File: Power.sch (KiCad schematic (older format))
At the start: 13 parts

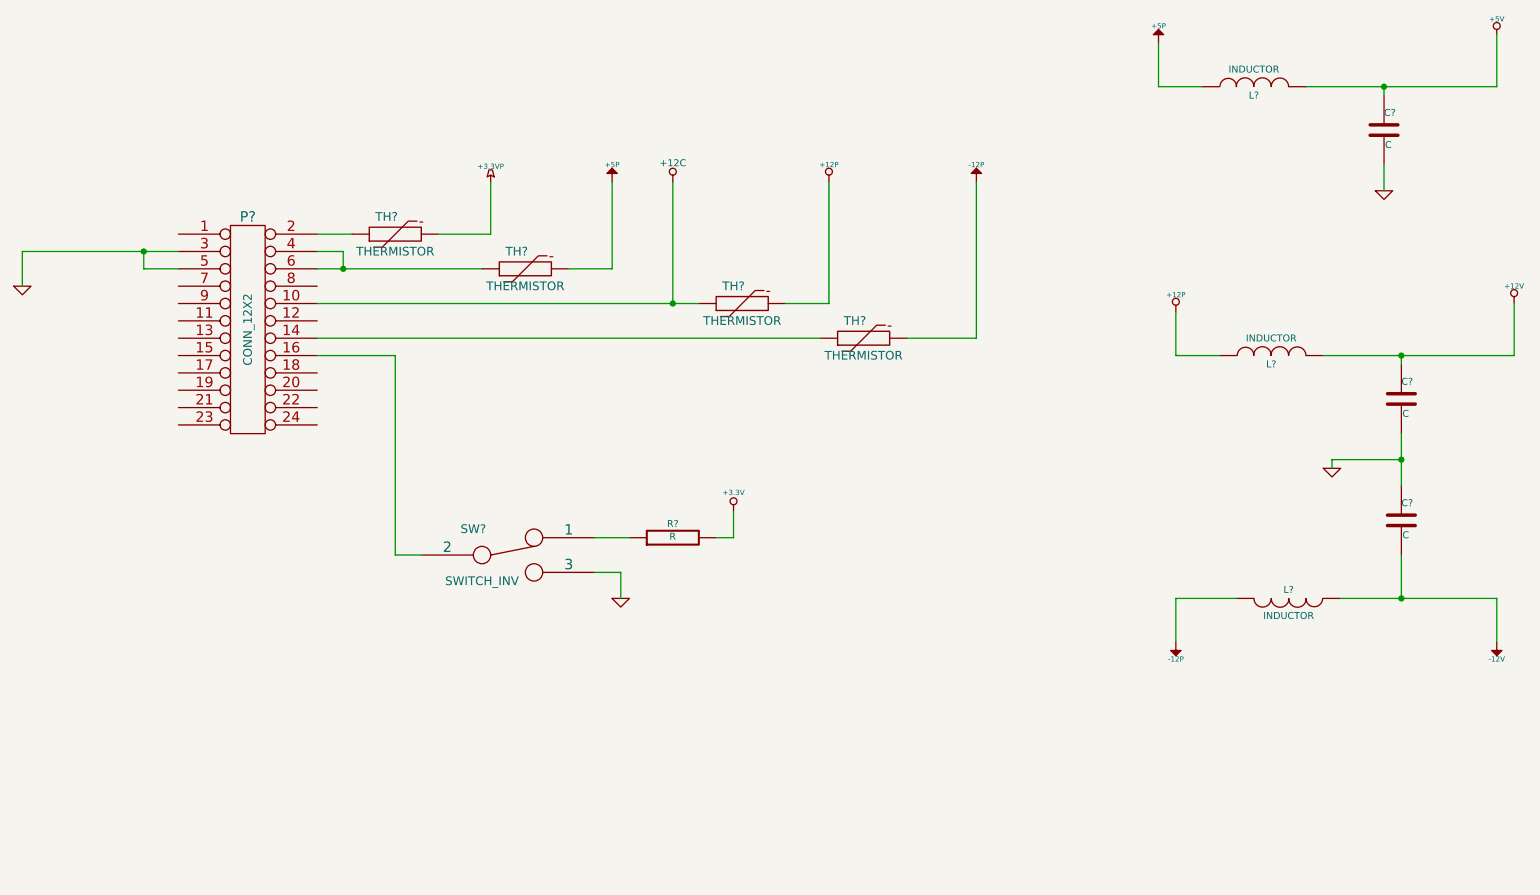
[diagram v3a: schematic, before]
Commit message: Relay module association and placement
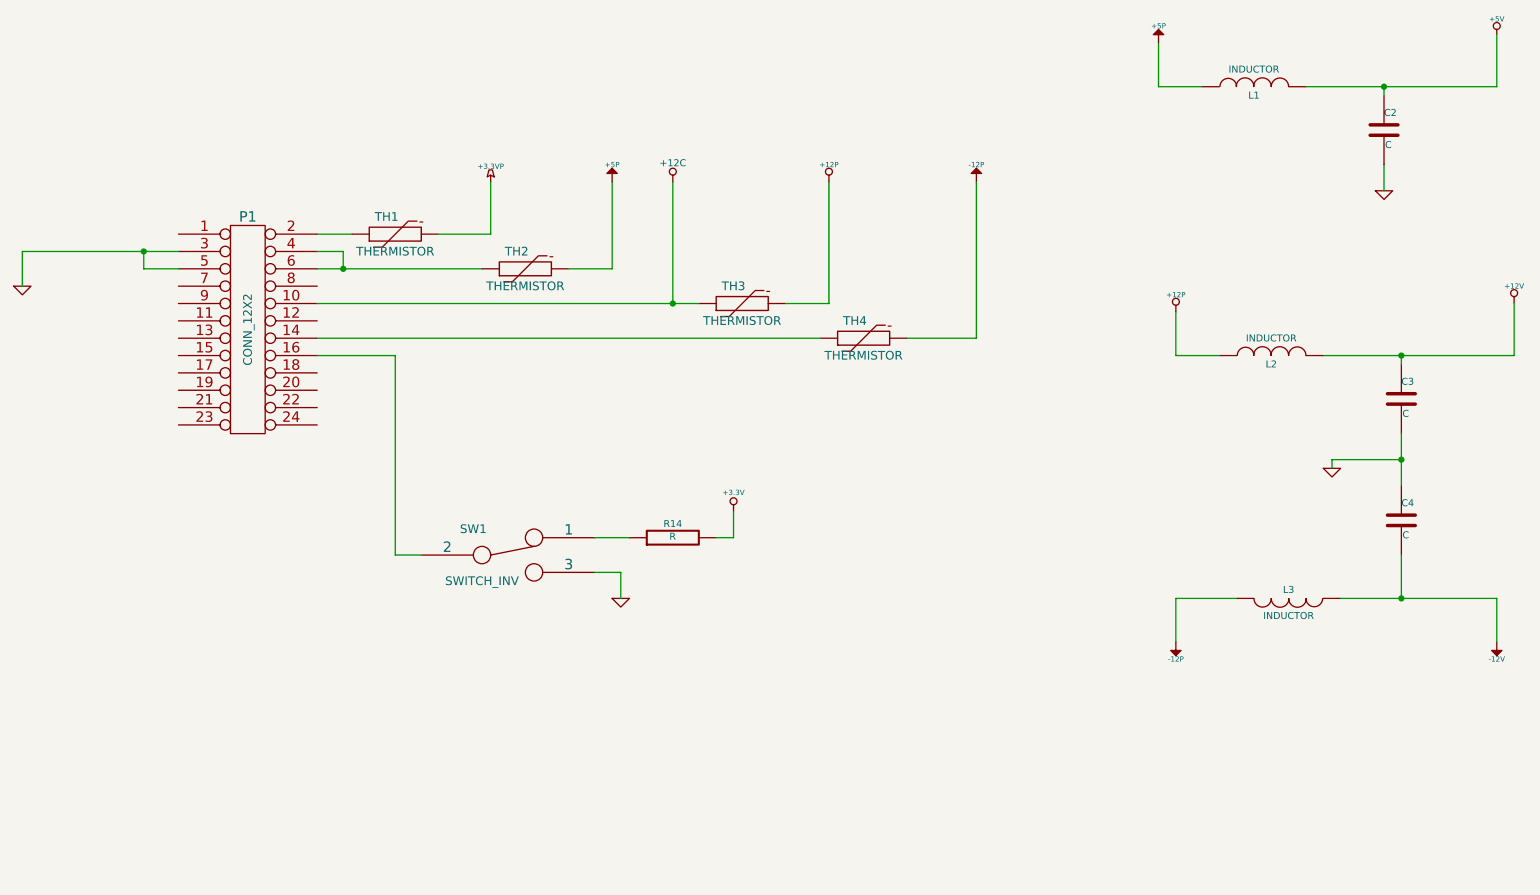
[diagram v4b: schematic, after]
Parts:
- gave numbers to parts that had none: 13
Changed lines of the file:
@@
 Sheet 4 9
 Title ""
-Date "18 feb 2014"
+Date "20 feb 2014"
 Rev ""
 Comp ""
@@
 $EndDescr
 $Comp
-L CONN_12X2 P?
+L CONN_12X2 P1
 U 1 1 52F67DF4
 P 2900 2400
-F 0 "P?" H 2900 3050 60  0000 C CNN
+F 0 "P1" H 2900 3050 60  0000 C CNN
 F 1 "CONN_12X2" V 2900 2400 50  0000 C CNN
 F 2 "" H 2900 2400 60  0000 C CNN
@@
 $EndComp
 $Comp
-L GND #PWR?
+L GND #PWR011
 U 1 1 52F67E5D
 P 1600 2150
-F 0 "#PWR?" H 1600 2150 30  0001 C CNN
+F 0 "#PWR011" H 1600 2150 30  0001 C CNN
 F 1 "GND" H 1600 2080 30  0001 C CNN
 F 2 "" H 1600 2150 60  0000 C CNN
@@
 $EndComp
 $Comp
-L SWITCH_INV SW?
+L SWITCH_INV SW1
 U 1 1 52F67EC9
 P 4400 3700
-F 0 "SW?" H 4200 3850 50  0000 C CNN
+F 0 "SW1" H 4200 3850 50  0000 C CNN
 F 1 "SWITCH_INV" H 4250 3550 50  0000 C CNN
 F 2 "~" H 4400 3700 60  0000 C CNN
@@
 	7100 2450 6700 2450
 $Comp
-L +12P #PWR?
+L +12P #PWR012
 U 1 1 52F68365
 P 6250 1550
-F 0 "#PWR?" H 6250 1520 30  0001 C CNN
+F 0 "#PWR012" H 6250 1520 30  0001 C CNN
 F 1 "+12P" H 6250 1650 30  0000 C CNN
 F 2 "" H 6250 1550 60  0000 C CNN
@@
 $EndComp
 $Comp
-L -12P #PWR?
+L -12P #PWR013
 U 1 1 52F68398
 P 7100 1550
-F 0 "#PWR?" H 7100 1680 20  0001 C CNN
+F 0 "#PWR013" H 7100 1680 20  0001 C CNN
 F 1 "-12P" H 7100 1650 30  0000 C CNN
 F 2 "" H 7100 1550 60  0000 C CNN
@@
 	3750 3700 3900 3700
 $Comp
-L GND #PWR?
+L GND #PWR014
 U 1 1 52F6840F
 P 5050 3950
-F 0 "#PWR?" H 5050 3950 30  0001 C CNN
+F 0 "#PWR014" H 5050 3950 30  0001 C CNN
 F 1 "GND" H 5050 3880 30  0001 C CNN
 F 2 "" H 5050 3950 60  0000 C CNN
@@
 	5050 3800 5050 3950
 $Comp
-L R R?
+L R R14
 U 1 1 52F6842F
 P 5350 3600
-F 0 "R?" V 5430 3600 40  0000 C CNN
+F 0 "R14" V 5430 3600 40  0000 C CNN
 F 1 "R" V 5357 3601 40  0000 C CNN
 F 2 "~" V 5280 3600 30  0000 C CNN
@@
 	3750 2550 3750 3700
 $Comp
-L +3.3V #PWR?
+L +3.3V #PWR015
 U 1 1 52F684A9
 P 5700 3450
-F 0 "#PWR?" H 5700 3410 30  0001 C CNN
+F 0 "#PWR015" H 5700 3410 30  0001 C CNN
 F 1 "+3.3V" H 5700 3560 30  0000 C CNN
 F 2 "" H 5700 3450 60  0000 C CNN
@@
 	5700 3600 5700 3450
 $Comp
-L +12P #PWR?
+L +12P #PWR016
 U 1 1 52F684CA
 P 8250 2300
-F 0 "#PWR?" H 8250 2270 30  0001 C CNN
+F 0 "#PWR016" H 8250 2270 30  0001 C CNN
 F 1 "+12P" H 8250 2400 30  0000 C CNN
 F 2 "" H 8250 2300 60  0000 C CNN
@@
 $EndComp
 $Comp
-L GND #PWR?
+L GND #PWR017
 U 1 1 52F684D0
 P 9150 3200
-F 0 "#PWR?" H 9150 3200 30  0001 C CNN
+F 0 "#PWR017" H 9150 3200 30  0001 C CNN
 F 1 "GND" H 9150 3130 30  0001 C CNN
 F 2 "" H 9150 3200 60  0000 C CNN
@@
 $EndComp
 $Comp
-L -12P #PWR?
+L -12P #PWR018
 U 1 1 52F684D6
 P 8250 4200
-F 0 "#PWR?" H 8250 4330 20  0001 C CNN
+F 0 "#PWR018" H 8250 4330 20  0001 C CNN
 F 1 "-12P" H 8250 4300 30  0000 C CNN
 F 2 "" H 8250 4200 60  0000 C CNN
@@
 $EndComp
 $Comp
-L INDUCTOR L?
+L INDUCTOR L2
 U 1 1 52F684DE
 P 8800 2550
-F 0 "L?" V 8750 2550 40  0000 C CNN
+F 0 "L2" V 8750 2550 40  0000 C CNN
 F 1 "INDUCTOR" V 8900 2550 40  0000 C CNN
 F 2 "~" H 8800 2550 60  0000 C CNN
@@
 $EndComp
 $Comp
-L INDUCTOR L?
+L INDUCTOR L3
 U 1 1 52F684EB
 P 8900 3950
-F 0 "L?" V 8850 3950 40  0000 C CNN
+F 0 "L3" V 8850 3950 40  0000 C CNN
 F 1 "INDUCTOR" V 9000 3950 40  0000 C CNN
 F 2 "~" H 8900 3950 60  0000 C CNN
@@
 $EndComp
 $Comp
-L C C?
+L C C3
 U 1 1 52F68508
 P 9550 2800
-F 0 "C?" H 9550 2900 40  0000 L CNN
+F 0 "C3" H 9550 2900 40  0000 L CNN
 F 1 "C" H 9556 2715 40  0000 L CNN
 F 2 "~" H 9588 2650 30  0000 C CNN
@@
 $EndComp
 $Comp
-L C C?
+L C C4
 U 1 1 52F68515
 P 9550 3500
-F 0 "C?" H 9550 3600 40  0000 L CNN
+F 0 "C4" H 9550 3600 40  0000 L CNN
 F 1 "C" H 9556 3415 40  0000 L CNN
 F 2 "~" H 9588 3350 30  0000 C CNN
@@
 	8250 3950 8600 3950
 $Comp
-L -12V #PWR?
+L -12V #PWR019
 U 1 1 52F68656
 P 10100 4200
-F 0 "#PWR?" H 10100 4330 20  0001 C CNN
+F 0 "#PWR019" H 10100 4330 20  0001 C CNN
 F 1 "-12V" H 10100 4300 30  0000 C CNN
 F 2 "" H 10100 4200 60  0000 C CNN
@@
 $EndComp
 $Comp
-L +12V #PWR?
+L +12V #PWR020
 U 1 1 52F68665
 P 10200 2250
-F 0 "#PWR?" H 10200 2200 20  0001 C CNN
+F 0 "#PWR020" H 10200 2200 20  0001 C CNN
 F 1 "+12V" H 10200 2350 30  0000 C CNN
 F 2 "" H 10200 2250 60  0000 C CNN
@@
 Connection ~ 9550 3950
 $Comp
-L +12C #PWR?
+L +12C #PWR021
 U 1 1 52F7CE7C
 P 5350 1550
-F 0 "#PWR?" H 5350 1520 30  0001 C CNN
+F 0 "#PWR021" H 5350 1520 30  0001 C CNN
 F 1 "+12C" H 5350 1660 40  0000 C CNN
 F 2 "" H 5350 1550 60  0000 C CNN
@@
 Connection ~ 5350 2250
 $Comp
-L THERMISTOR TH?
+L THERMISTOR TH1
 U 1 1 52F7D3F0
 P 3750 1850
-F 0 "TH?" V 3850 1900 50  0000 C CNN
+F 0 "TH1" V 3850 1900 50  0000 C CNN
 F 1 "THERMISTOR" V 3650 1850 50  0000 C CNN
 F 2 "~" H 3750 1850 60  0000 C CNN
@@
 $EndComp
 $Comp
-L THERMISTOR TH?
+L THERMISTOR TH2
 U 1 1 52F7D3FF
 P 4500 2050
-F 0 "TH?" V 4600 2100 50  0000 C CNN
+F 0 "TH2" V 4600 2100 50  0000 C CNN
 F 1 "THERMISTOR" V 4400 2050 50  0000 C CNN
 F 2 "~" H 4500 2050 60  0000 C CNN
@@
 $EndComp
 $Comp
-L THERMISTOR TH?
+L THERMISTOR TH3
 U 1 1 52F7D40E
 P 5750 2250
-F 0 "TH?" V 5850 2300 50  0000 C CNN
+F 0 "TH3" V 5850 2300 50  0000 C CNN
 F 1 "THERMISTOR" V 5650 2250 50  0000 C CNN
 F 2 "~" H 5750 2250 60  0000 C CNN
@@
 $EndComp
 $Comp
-L THERMISTOR TH?
+L THERMISTOR TH4
 U 1 1 52F7D41D
 P 6450 2450
-F 0 "TH?" V 6550 2500 50  0000 C CNN
+F 0 "TH4" V 6550 2500 50  0000 C CNN
 F 1 "THERMISTOR" V 6350 2450 50  0000 C CNN
 F 2 "~" H 6450 2450 60  0000 C CNN
@@
 $EndComp
 $Comp
-L +5P #PWR?
+L +5P #PWR13
 U 1 1 5302A929
 P 5000 1550
-F 0 "#PWR?" H 5000 1680 20  0001 C CNN
+F 0 "#PWR13" H 5000 1680 20  0001 C CNN
 F 1 "+5P" H 5000 1650 30  0000 C CNN
 F 2 "" H 5000 1550 60  0000 C CNN
@@
 $EndComp
 $Comp
-L +3.3VP #PWR?
+L +3.3VP #PWR022
 U 1 1 5302A942
 P 4300 1550
-F 0 "#PWR?" H 4350 1580 20  0001 C CNN
+F 0 "#PWR022" H 4350 1580 20  0001 C CNN
 F 1 "+3.3VP" H 4300 1640 30  0000 C CNN
 F 2 "" H 4300 1550 60  0000 C CNN
@@
 $EndComp
 $Comp
-L INDUCTOR L?
+L INDUCTOR L1
 U 1 1 5302A984
 P 8700 1000
-F 0 "L?" V 8650 1000 40  0000 C CNN
+F 0 "L1" V 8650 1000 40  0000 C CNN
 F 1 "INDUCTOR" V 8800 1000 40  0000 C CNN
 F 2 "~" H 8700 1000 60  0000 C CNN
@@
 $EndComp
 $Comp
-L C C?
+L C C2
 U 1 1 5302A98A
 P 9450 1250
-F 0 "C?" H 9450 1350 40  0000 L CNN
+F 0 "C2" H 9450 1350 40  0000 L CNN
 F 1 "C" H 9456 1165 40  0000 L CNN
 F 2 "~" H 9488 1100 30  0000 C CNN
@@
 Connection ~ 9450 1000
 $Comp
-L GND #PWR?
+L GND #PWR023
 U 1 1 5302A99D
 P 9450 1600
-F 0 "#PWR?" H 9450 1600 30  0001 C CNN
+F 0 "#PWR023" H 9450 1600 30  0001 C CNN
 F 1 "GND" H 9450 1530 30  0001 C CNN
 F 2 "" H 9450 1600 60  0000 C CNN
@@
 	9450 1600 9450 1450
 $Comp
-L +5P #PWR?
+L +5P #PWR19
 U 1 1 5302A9DA
 P 8150 750
-F 0 "#PWR?" H 8150 880 20  0001 C CNN
+F 0 "#PWR19" H 8150 880 20  0001 C CNN
 F 1 "+5P" H 8150 850 30  0000 C CNN
 F 2 "" H 8150 750 60  0000 C CNN
@@
 $EndComp
 $Comp
-L +5V #PWR?
+L +5V #PWR024
 U 1 1 5302A9E9
 P 10100 700
-F 0 "#PWR?" H 10100 790 20  0001 C CNN
+F 0 "#PWR024" H 10100 790 20  0001 C CNN
 F 1 "+5V" H 10100 790 30  0000 C CNN
 F 2 "" H 10100 700 60  0000 C CNN

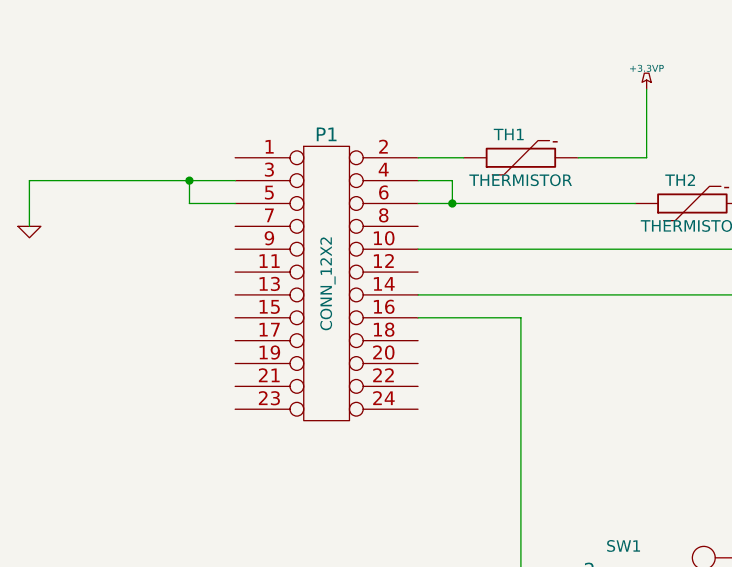
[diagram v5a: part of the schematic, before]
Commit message: Terminal block and Arduino: assc/placement
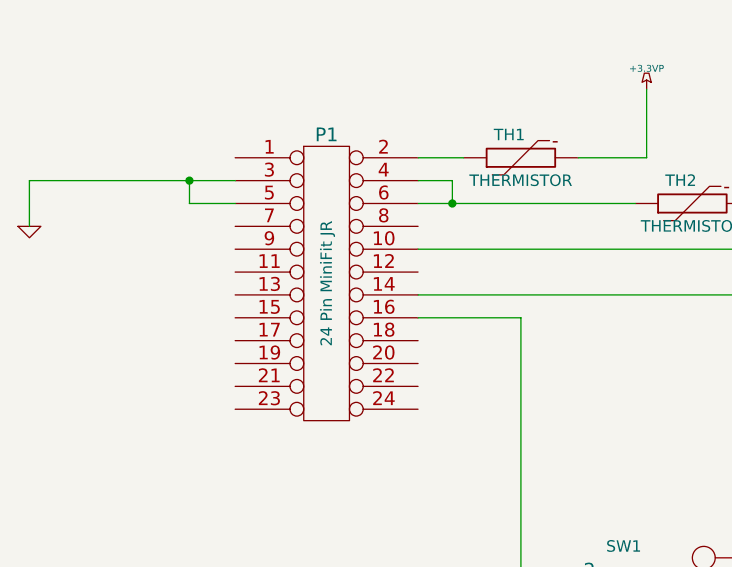
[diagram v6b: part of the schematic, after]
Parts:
- P1: value CONN_12X2 -> 24 Pin MiniFit JR; MFG Name (none) -> Molex
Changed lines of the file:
@@
 $Descr A4 11693 8268
 encoding utf-8
-Sheet 4 9
+Sheet 2 9
 Title ""
-Date "21 feb 2014"
+Date "22 feb 2014"
 Rev ""
 Comp ""
@@
 P 2900 2400
 F 0 "P1" H 2900 3050 60  0000 C CNN
-F 1 "CONN_12X2" V 2900 2400 50  0000 C CNN
+F 1 "24 Pin MiniFit JR" V 2900 2400 50  0000 C CNN
 F 2 "" H 2900 2400 60  0000 C CNN
 F 3 "" H 2900 2400 60  0000 C CNN
+F 4 "Molex" H 2900 2400 60  0001 C CNN "MFG Name"
 	1    2900 2400
 	1    0    0    -1

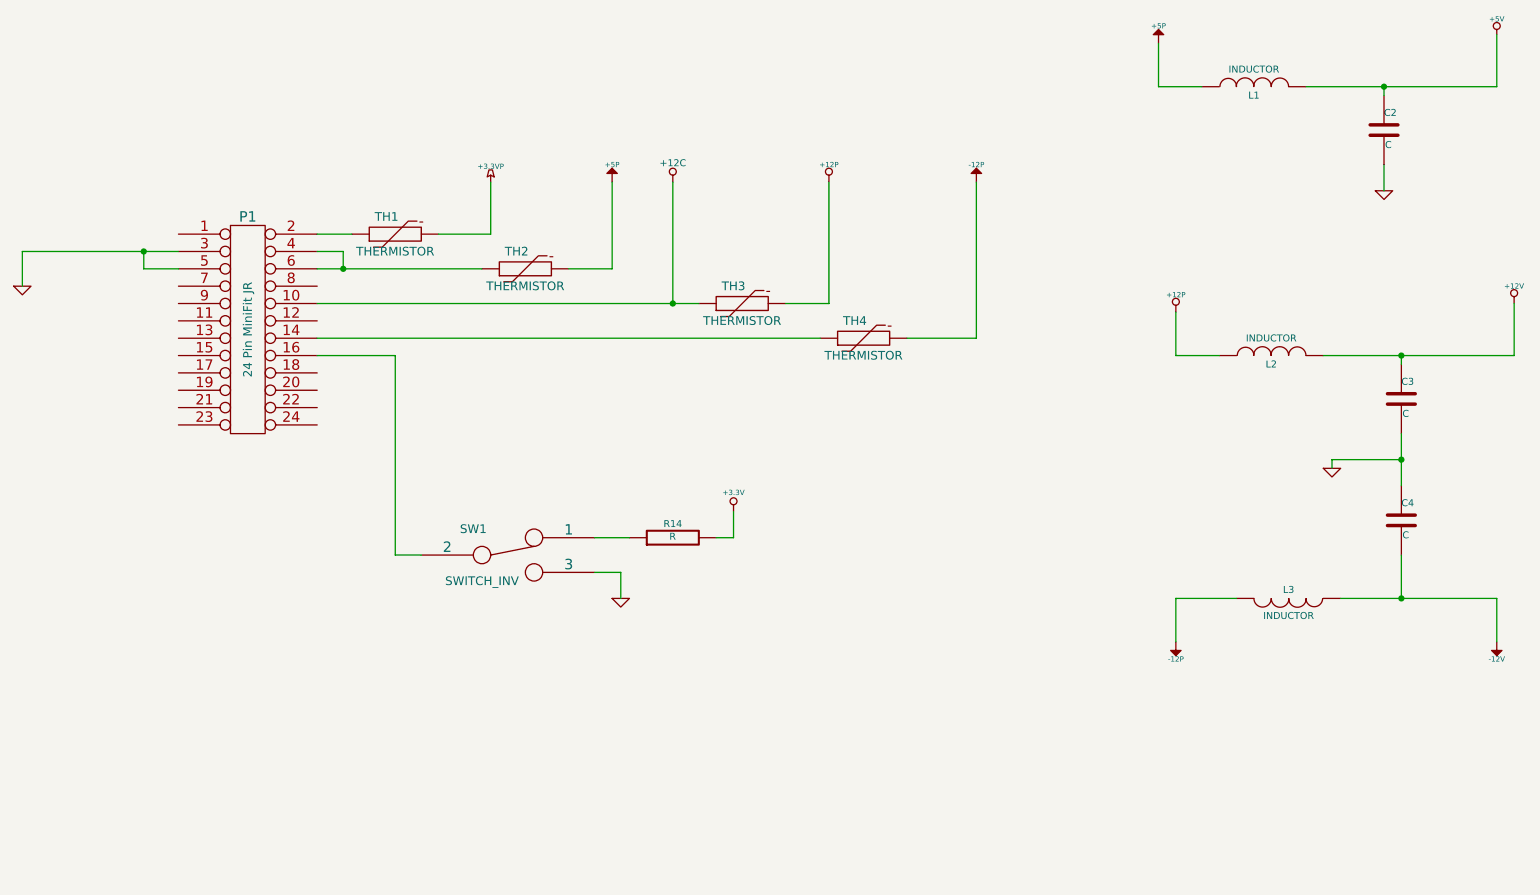
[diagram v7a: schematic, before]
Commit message: Power protection and filter: assc/placement
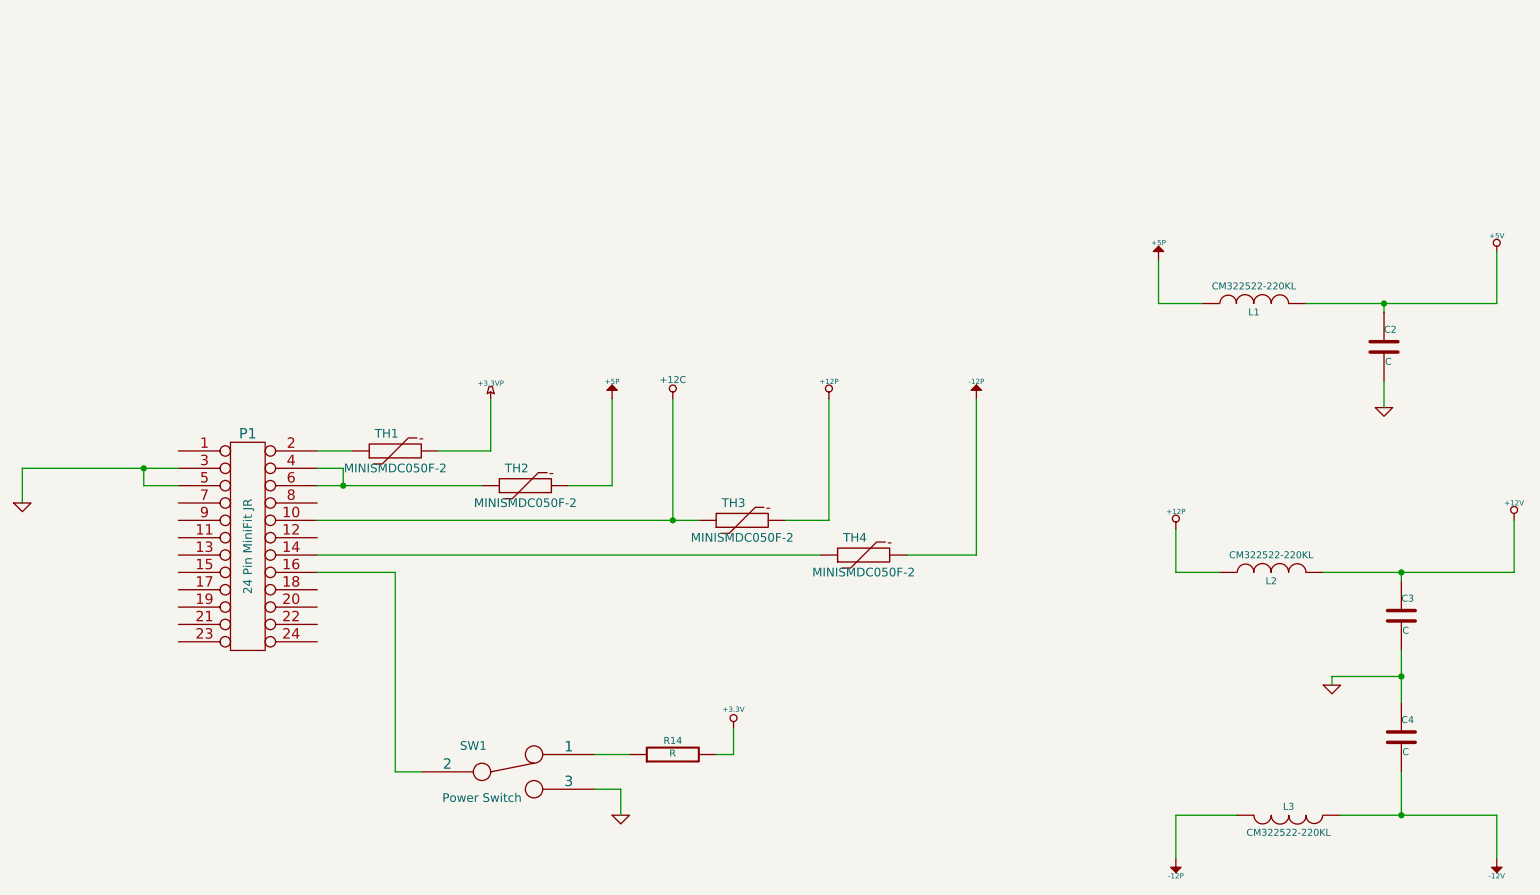
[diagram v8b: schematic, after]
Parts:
- L1, L2, L3: value INDUCTOR -> CM322522-220KL; MFG Name (none) -> Bournes; MFG Part Number (none) -> CM322522-220KL
- SW1: value SWITCH_INV -> Power Switch; MFG Name (none) -> C&K Components; MFG Part Number (none) -> OS102011MA1QN1
- TH1, TH2, TH3, TH4: value THERMISTOR -> MINISMDC050F-2; MFG Name (none) -> TE Connectivity; MFG Part Number (none) -> MINISMDC050F-2
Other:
- moved on the sheet: C2, C3, C4, L1, L2, L3, P1, R14, SW1, TH1, TH2, TH3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
